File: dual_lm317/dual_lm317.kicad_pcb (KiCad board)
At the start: 2 copper layers, 55 x 25 mm, 19 parts, among them J1 Conn_01x02_Male, J2 Conn_01x02_Male, U1 LM317_TO-220, U2 LT3080xST, U3 LT3080xST

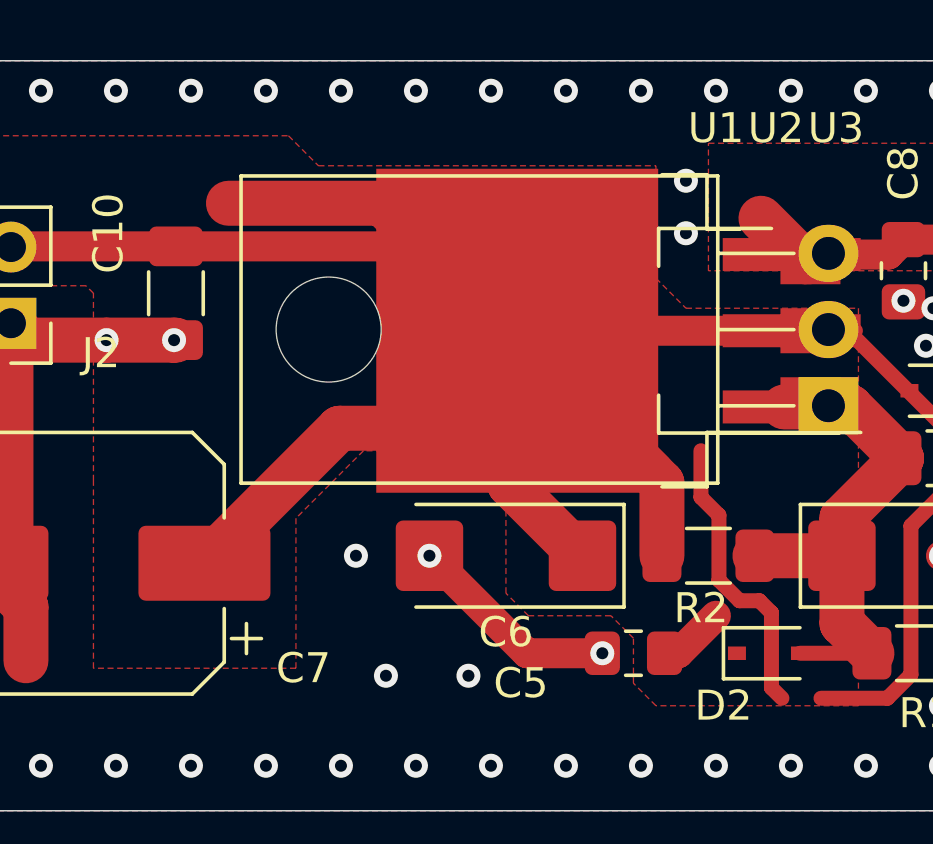
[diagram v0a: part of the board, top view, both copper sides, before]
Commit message: Fix library version mismatch
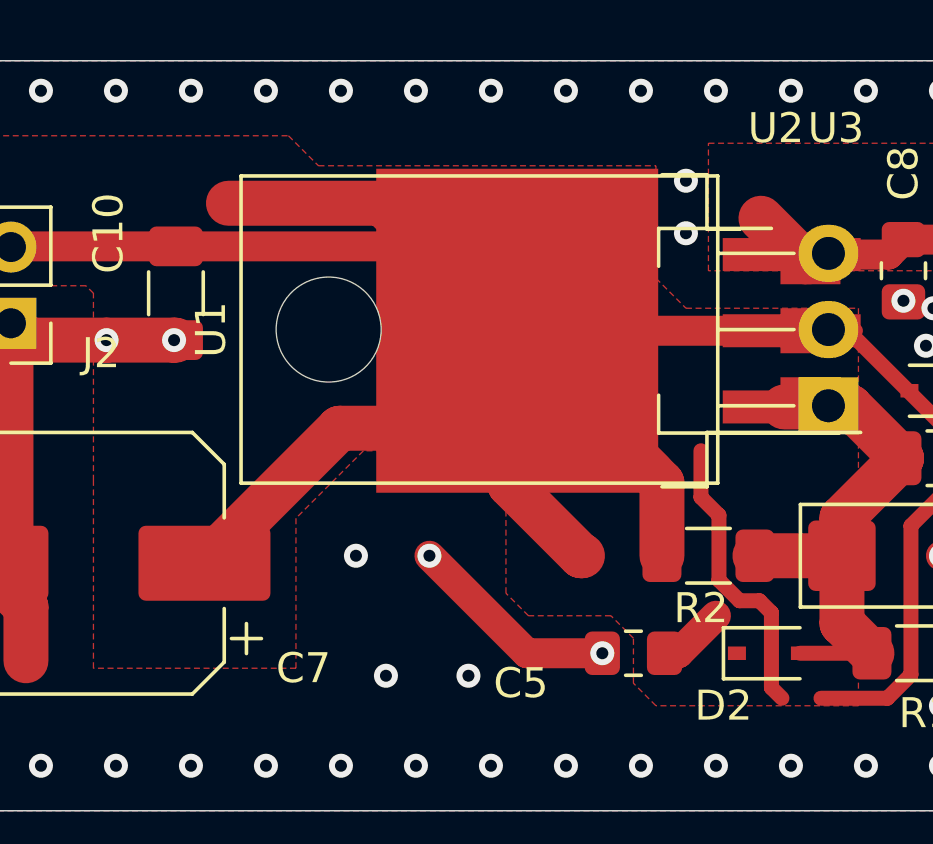
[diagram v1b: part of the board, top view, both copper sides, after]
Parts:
- removed C6: Tant 10uF, Capacitor_Tantalum_SMD:CP_EIA-6032-15_Kemet-U_Pad2.25x2.35mm_HandSolder
- U1: value LM317_TO-220 -> LM317_3PinPackage

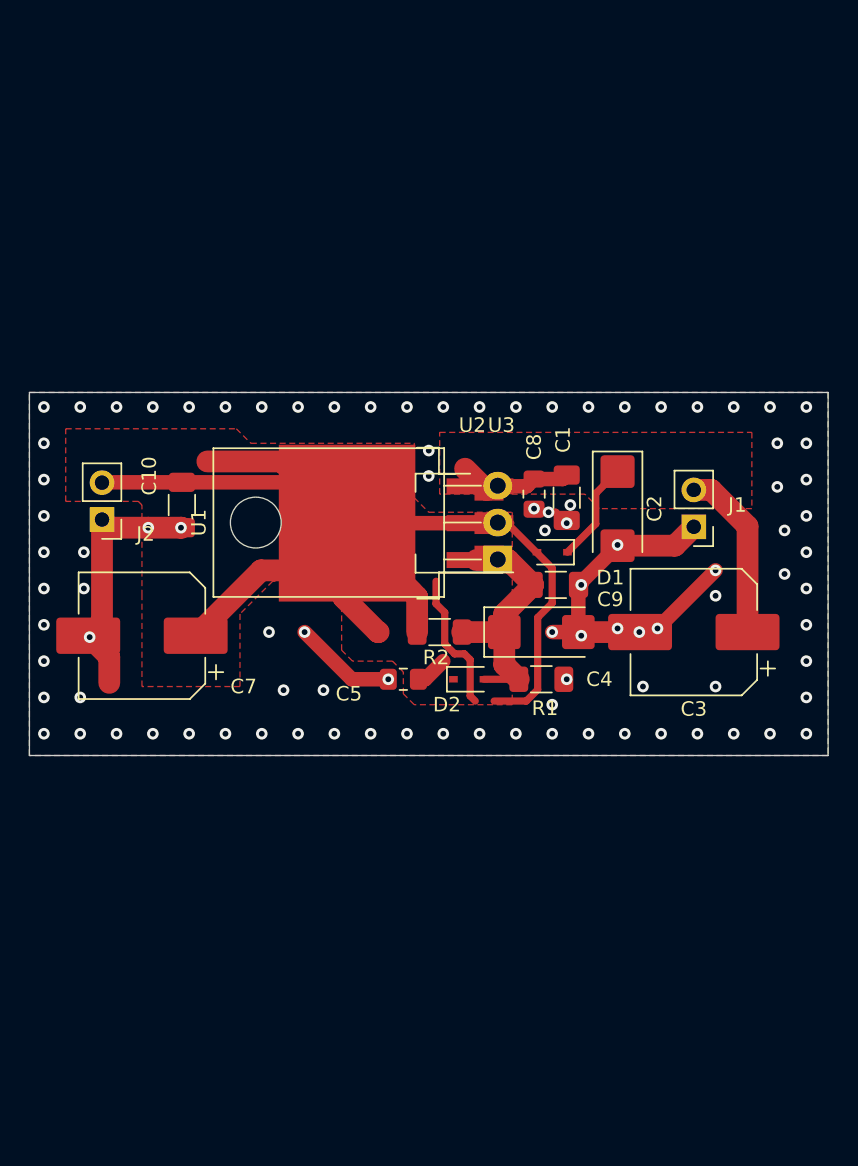
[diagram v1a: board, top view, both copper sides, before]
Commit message: migrate heirachycal sheets
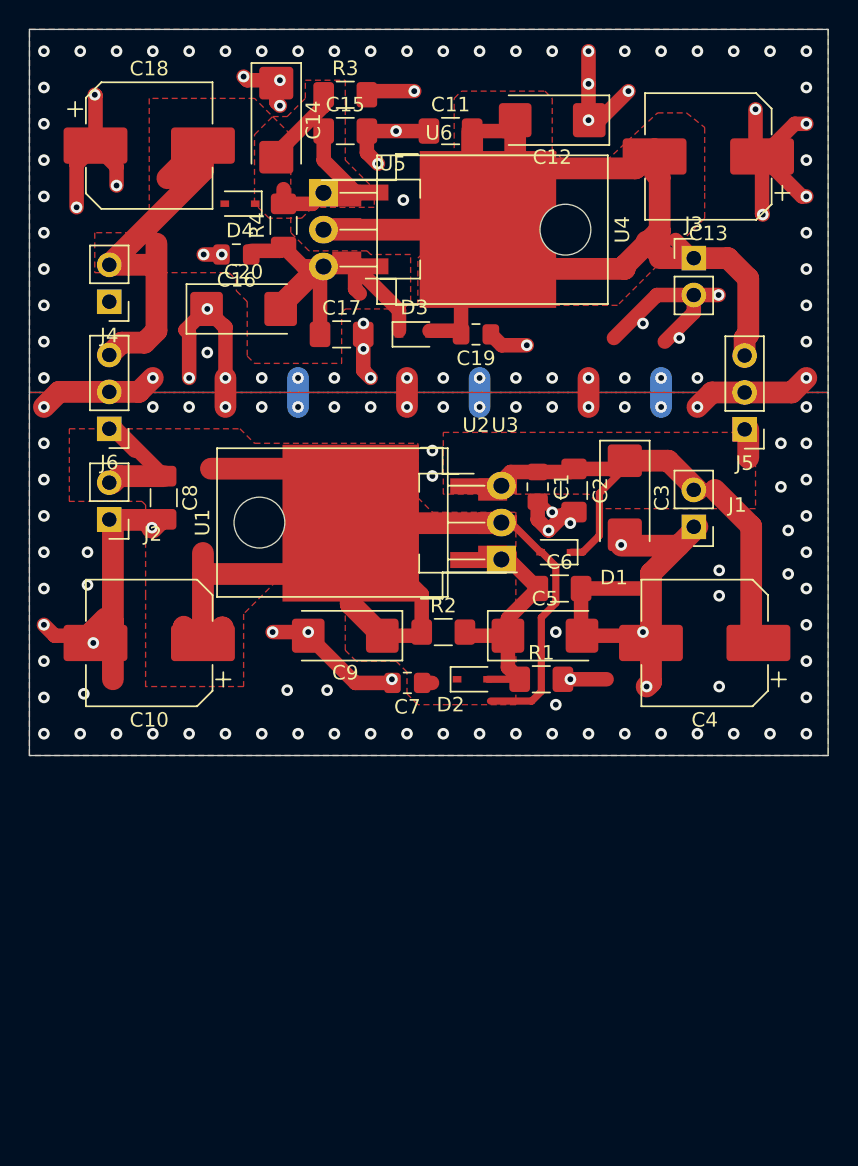
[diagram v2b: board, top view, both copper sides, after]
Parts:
- added C11: 1u, Capacitor_SMD:C_1206_3216Metric_Pad1.42x1.75mm_HandSolder, F.Cu at (131.5, 54.5)
- added C12: Tant 10uF, Capacitor_Tantalum_SMD:CP_EIA-6032-15_Kemet-U_Pad2.25x2.35mm_HandSolder, F.Cu at (138.5, 53.8)
- added C13: Electrolytic, Capacitor_SMD:CP_Elec_8x10.5, F.Cu at (149.2, 56.2)
- added C14: Tant 10uF, Capacitor_Tantalum_SMD:CP_EIA-6032-15_Kemet-U_Pad2.25x2.35mm_HandSolder, F.Cu at (119.5, 53.8)
- added C15: 0.01u c0g, Capacitor_SMD:C_1206_3216Metric_Pad1.42x1.75mm_HandSolder, F.Cu at (124.2, 54.5)
- added C16: 0.1u, Capacitor_SMD:C_0805_2012Metric_Pad1.15x1.40mm_HandSolder, F.Cu at (116.8, 63.0)
- added C17: 1u, Capacitor_SMD:C_1206_3216Metric_Pad1.42x1.75mm_HandSolder, F.Cu at (124.0, 68.5)
- added C18: Electrolytic, Capacitor_SMD:CP_Elec_8x10.5, F.Cu at (110.8, 55.5)
- added C19: 0.1u, Capacitor_SMD:C_0805_2012Metric_Pad1.15x1.40mm_HandSolder, F.Cu at (133.2, 68.5)
- added C20: Tant 10uF, Capacitor_Tantalum_SMD:CP_EIA-6032-15_Kemet-U_Pad2.25x2.35mm_HandSolder, F.Cu at (117.2, 66.8)
- added C6: 0.01u c0g, Capacitor_SMD:C_1206_3216Metric_Pad1.42x1.75mm_HandSolder, F.Cu at (139.0, 86.0)
- added D3: D, Diode_SMD:D_SOD-323, F.Cu at (129.0, 68.5)
- added D4: D, Diode_SMD:D_SOD-323, F.Cu at (117.0, 59.5)
- added J3: Conn_01x02_Male, Connector_PinHeader_2.54mm:PinHeader_1x02_P2.54mm_Vertical, F.Cu at (148.2, 63.2)
- added J4: Conn_01x02_Male, Connector_PinHeader_2.54mm:PinHeader_1x02_P2.54mm_Vertical, F.Cu at (108.0, 66.2)
- added J5: Conn_01x03_Male, Connector_PinHeader_2.54mm:PinHeader_1x03_P2.54mm_Vertical, F.Cu at (151.8, 75.0)
- added J6: Conn_01x03_Male, Connector_PinHeader_2.54mm:PinHeader_1x03_P2.54mm_Vertical, F.Cu at (108.0, 75.0)
- added R3: R, Resistor_SMD:R_1206_3216Metric_Pad1.42x1.75mm_HandSolder, F.Cu at (124.2, 52.0)
- added R4: R, Resistor_SMD:R_1206_3216Metric_Pad1.42x1.75mm_HandSolder, F.Cu at (120.0, 61.0)
- added U4: LM337_TO220, Package_TO_SOT_THT:TO-220-3_Horizontal_TabDown, F.Cu at (122.8, 58.8)
- added U5: LM337_SOT223, Package_TO_SOT_SMD:SOT-223-3_TabPin2, F.Cu at (127.5, 61.2)
- added U6: LM337_TO263, Package_TO_SOT_SMD:TO-263-2, F.Cu at (130.7, 61.3)
- C1: value 1u -> 0.1u; footprint Capacitor_SMD:C_1206_3216Metric_Pad1.33x1.80mm_HandSolder -> Capacitor_SMD:C_0805_2012Metric_Pad1.15x1.40mm_HandSolder
- C10: value 1u -> Electrolytic; footprint Capacitor_SMD:C_1206_3216Metric_Pad1.33x1.80mm_HandSolder -> Capacitor_SMD:CP_Elec_8x10.5
- C2: value Tant 10uF -> 1u; footprint Capacitor_Tantalum_SMD:CP_EIA-6032-15_Kemet-U_Pad2.25x2.35mm_HandSolder -> Capacitor_SMD:C_1206_3216Metric_Pad1.42x1.75mm_HandSolder
- C3: value Electrolytic -> Tant 10uF; footprint Capacitor_SMD:CP_Elec_8x10.5 -> Capacitor_Tantalum_SMD:CP_EIA-6032-15_Kemet-U_Pad2.25x2.35mm_HandSolder
- C4: value Tant 10uF -> Electrolytic; footprint Capacitor_Tantalum_SMD:CP_EIA-6032-15_Kemet-U_Pad2.25x2.35mm_HandSolder -> Capacitor_SMD:CP_Elec_8x10.5
- C5: value 0.1u -> Tant 10uF; footprint Capacitor_SMD:C_0805_2012Metric_Pad1.18x1.45mm_HandSolder -> Capacitor_Tantalum_SMD:CP_EIA-6032-15_Kemet-U_Pad2.25x2.35mm_HandSolder
- C7: value Electrolytic -> 0.1u; footprint Capacitor_SMD:CP_Elec_8x10.5 -> Capacitor_SMD:C_0805_2012Metric_Pad1.15x1.40mm_HandSolder
- C8: value 0.1u -> 1u; footprint Capacitor_SMD:C_0805_2012Metric_Pad1.18x1.45mm_HandSolder -> Capacitor_SMD:C_1206_3216Metric_Pad1.42x1.75mm_HandSolder
- C9: value 0.01u c0g -> Tant 10uF; footprint Capacitor_SMD:C_1206_3216Metric_Pad1.33x1.80mm_HandSolder -> Capacitor_Tantalum_SMD:CP_EIA-6032-15_Kemet-U_Pad2.25x2.35mm_HandSolder
- R1, R2: footprint Resistor_SMD:R_1206_3216Metric_Pad1.30x1.75mm_HandSolder -> Resistor_SMD:R_1206_3216Metric_Pad1.42x1.75mm_HandSolder
- moved C8 25.5 mm to (111.8, 79.8)
- moved C7 18.6 mm to (128.5, 92.5)
- moved C9 14.9 mm to (124.2, 89.2), turned to 180 degrees
- moved C4 11.3 mm to (149.0, 89.8), turned to 180 degrees
- moved C3 10.4 mm to (143.5, 79.8), turned to 270 degrees
- moved C5 10.2 mm to (138.0, 89.2), turned to 0 degrees
- moved C10 9.76 mm to (110.8, 89.8), turned to 180 degrees
- moved C2 3.25 mm to (140.0, 79.2)
- moved C1 2.14 mm to (137.5, 79.0)
- moved J2 0.50 mm to (108.0, 81.2)
- moved D1 0.25 mm to (138.8, 83.5)
- moved D2 0.25 mm to (133.0, 92.2)
- moved R2 0.25 mm to (131.0, 89.0)
- moved U1 0.25 mm to (135.0, 84.0)
- moved U2 0.25 mm to (131.2, 81.5)
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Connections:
- C4 pad 1: /VadjA -> /VinA
- C5 pad 1: /VoutA -> /VadjA
- C8 pad 1: /VinA -> /VoutA
- C9 pad 1: /VadjA -> /VoutA
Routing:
- net /GNDA: track 52.9 -> 179.3 mm, vias 95 -> 165
- net /VinAN: track 0.00 -> 86.9 mm
- net /VoutAN: track 0.00 -> 51.1 mm
- net /VadjAN: track 0.00 -> 14.6 mm
- net /VoutA: track 107.5 -> 94.4 mm
- net /VinA: track 27.6 -> 36.0 mm
- added copper zone on F.Cu, net /VadjAN
- added copper zone on F.Cu, net /VinAN
- added copper zone on F.Cu, net /VoutAN
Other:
- board size 55 x 25 mm -> 55 x 50 mm

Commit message: Relay array board; Last checkup; Gerberfile updates
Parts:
- added C21: 0.1u, Capacitor_SMD:C_0805_2012Metric_Pad1.15x1.40mm_HandSolder, F.Cu at (137.5, 105.2)
- added C22: 1u, Capacitor_SMD:C_1206_3216Metric_Pad1.42x1.75mm_HandSolder, F.Cu at (140.0, 105.5)
- added C23: Tant 10uF, Capacitor_Tantalum_SMD:CP_EIA-6032-15_Kemet-U_Pad2.25x2.35mm_HandSolder, F.Cu at (143.5, 106.0)
- added C24: Electrolytic, Capacitor_SMD:CP_Elec_8x10.5, F.Cu at (149.0, 116.0)
- added C25: Tant 10uF, Capacitor_Tantalum_SMD:CP_EIA-6032-15_Kemet-U_Pad2.25x2.35mm_HandSolder, F.Cu at (138.0, 115.5)
- added C26: 0.01u c0g, Capacitor_SMD:C_1206_3216Metric_Pad1.42x1.75mm_HandSolder, F.Cu at (139.0, 112.2)
- added C27: 0.1u, Capacitor_SMD:C_0805_2012Metric_Pad1.15x1.40mm_HandSolder, F.Cu at (128.5, 118.8)
- added C28: 1u, Capacitor_SMD:C_1206_3216Metric_Pad1.42x1.75mm_HandSolder, F.Cu at (111.8, 106.0)
- added C29: Tant 10uF, Capacitor_Tantalum_SMD:CP_EIA-6032-15_Kemet-U_Pad2.25x2.35mm_HandSolder, F.Cu at (124.2, 115.5)
- added C30: Electrolytic, Capacitor_SMD:CP_Elec_8x10.5, F.Cu at (110.8, 116.0)
- added D5: D, Diode_SMD:D_SOD-323, F.Cu at (138.8, 109.8)
- added D6: D, Diode_SMD:D_SOD-323, F.Cu at (133.0, 118.5)
- added J7: Conn_01x02_Male, Connector_PinHeader_2.54mm:PinHeader_1x02_P2.54mm_Vertical, F.Cu at (148.2, 108.0)
- added J8: Conn_01x02_Male, Connector_PinHeader_2.54mm:PinHeader_1x02_P2.54mm_Vertical, F.Cu at (108.0, 107.5)
- added R5: R, Resistor_SMD:R_1206_3216Metric_Pad1.42x1.75mm_HandSolder, F.Cu at (137.8, 118.5)
- added R6: R, Resistor_SMD:R_1206_3216Metric_Pad1.42x1.75mm_HandSolder, F.Cu at (131.0, 115.2)
- added U7: LM317_3PinPackage, Package_TO_SOT_THT:TO-220-3_Horizontal_TabDown, F.Cu at (135.0, 110.2)
- added U8: LT3080xST, Package_TO_SOT_SMD:SOT-223, F.Cu at (131.2, 107.8)
- added U9: LT3080xST, Package_TO_SOT_SMD:TO-263-3_TabPin4, F.Cu at (128.0, 107.8)
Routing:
- net /VoutB: track 0.00 -> 90.3 mm
- net /GNDB: track 0.00 -> 70.1 mm, vias 0 -> 88
- net /VinB: track 0.00 -> 36.0 mm
- net /VadjB: track 0.00 -> 17.3 mm
- added copper zone on B.Cu, net /GNDB
- added copper zone on F.Cu, net /GNDB
- added copper zone on F.Cu, net /VinB
- added copper zone on F.Cu, net /VoutB
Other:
- board size 55 x 50 mm -> 55 x 76.2 mm
